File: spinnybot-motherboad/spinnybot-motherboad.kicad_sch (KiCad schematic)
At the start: 6 parts

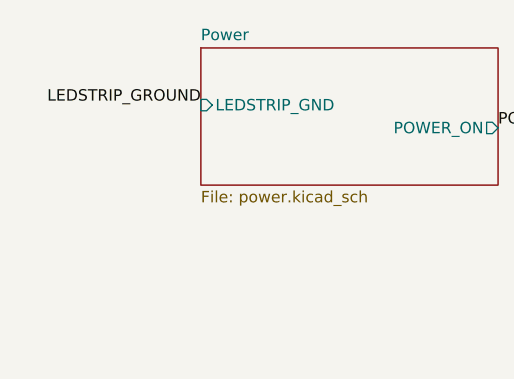
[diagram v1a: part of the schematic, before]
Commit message: fix LEDSTRIP_GND on the FET not being connected
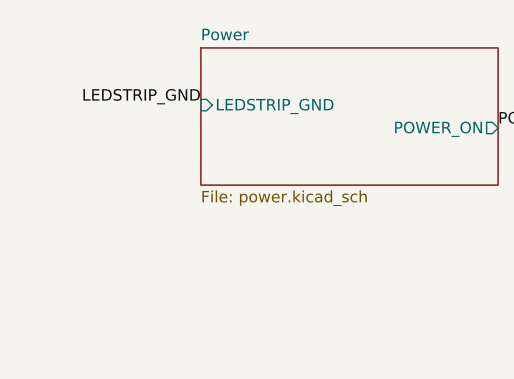
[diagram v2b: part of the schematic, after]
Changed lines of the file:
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@@
     (effects (font (size 1.27 1.27)) (justify left bottom))
   )
-  (label "LEDSTRIP_GROUND" (at 34.29 30.48 180)
+  (label "LEDSTRIP_GND" (at 34.29 30.48 180)
     (effects (font (size 1.27 1.27)) (justify right bottom))
   )

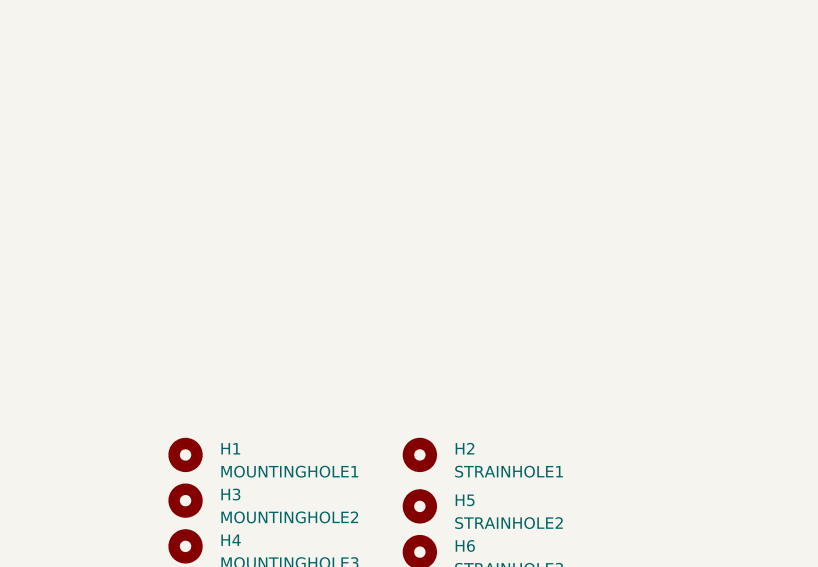
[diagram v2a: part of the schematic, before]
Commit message: tweaks to routing to make the ground plane more connected, add a top copper ground pour. move ESC FET.
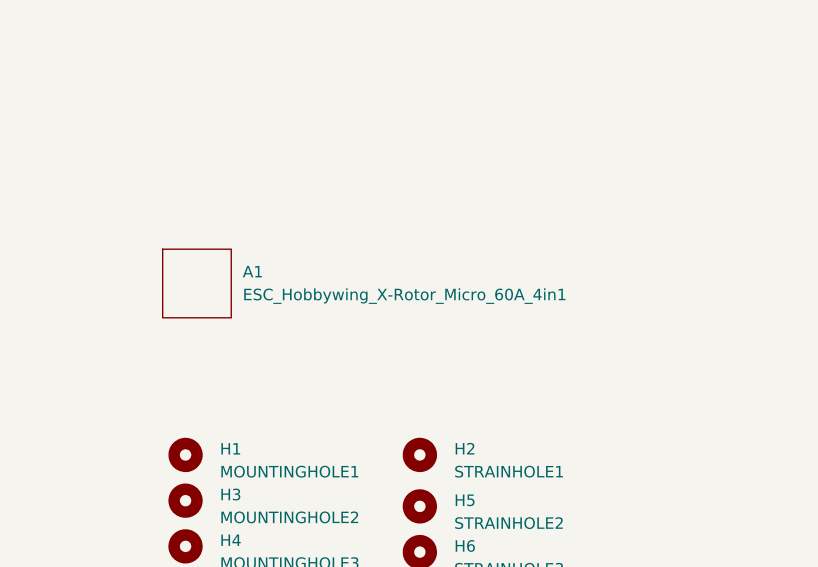
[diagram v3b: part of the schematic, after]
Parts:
- added A1: ESC_Hobbywing_X-Rotor_Micro_60A_4in1, esc_4in1:ESC_Hobbywing_X-Rotor_Micro_60A_4in1, symbol esc_4in1:ESC_Hobbywing_X-Rotor_Micro_60A_4in1
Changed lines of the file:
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@@
+    )
+  )
+  (symbol (lib_id "esc_4in1:ESC_Hobbywing_X-Rotor_Micro_60A_4in1") (at 50.8 134.62 0) (unit 1)
+    (in_bom yes) (on_board yes) (fields_autoplaced)
+    (property "Reference" "A1" (id 0) (at 55.88 133.3499 0)
+      (effects (font (size 1.27 1.27)) (justify left))
+    )
+    (property "Value" "ESC_Hobbywing_X-Rotor_Micro_60A_4in1" (id 1) (at 55.88 135.8899 0)
+      (effects (font (size 1.27 1.27)) (justify left))
+    )
+    (property "Footprint" "esc_4in1:ESC_Hobbywing_X-Rotor_Micro_60A_4in1" (id 2) (at 50.8 134.62 0)
+      (effects (font (size 1.27 1.27)) hide)
+    )
+    (property "Datasheet" "" (id 3) (at 50.8 134.62 0)
+      (effects (font (size 1.27 1.27)) hide)
     )
   )
@@
       (reference "#PWR0165") (unit 1) (value "GND") (footprint "")
     )
+    (path "/dd1316dc-7e5b-4c97-959e-6f6a1eeeb379/63151d2c-c4e6-4f75-94c3-ad61a0505834"
+      (reference "#PWR0166") (unit 1) (value "GND") (footprint "")
+    )
+    (path "/dd1316dc-7e5b-4c97-959e-6f6a1eeeb379/b6338eda-846c-4d61-9775-8bb6d52342a5"
+      (reference "#PWR0167") (unit 1) (value "GND") (footprint "")
+    )
+    (path "/4b51d6df-63b9-43fa-a920-8afa01c20793"
+      (reference "A1") (unit 1) (value "ESC_Hobbywing_X-Rotor_Micro_60A_4in1") (footprint "esc_4in1:ESC_Hobbywing_X-Rotor_Micro_60A_4in1")
+    )
     (path "/dd1316dc-7e5b-4c97-959e-6f6a1eeeb379/b5ccd461-2bb6-4e55-889d-c413ead53e97"

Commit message: adjust mounting holes to have pads and change locations
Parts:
- H2, H5, H6: footprint custom:MountingHole_3.3mm -> custom:StrainHole_3.3mm
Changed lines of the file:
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@@
       (effects (font (size 1.27 1.27)) (justify right))
     )
-    (property "Footprint" "custom:MountingHole_3.3mm" (id 2) (at 75.565 159.385 0)
+    (property "Footprint" "custom:StrainHole_3.3mm" (id 2) (at 75.565 159.385 0)
       (effects (font (size 1.27 1.27)) hide)
     )
@@
       (effects (font (size 1.27 1.27)) (justify right))
     )
-    (property "Footprint" "custom:MountingHole_3.3mm" (id 2) (at 75.565 153.67 0)
+    (property "Footprint" "custom:StrainHole_3.3mm" (id 2) (at 75.565 153.67 0)
       (effects (font (size 1.27 1.27)) hide)
     )
@@
       (effects (font (size 1.27 1.27)) (justify right))
     )
-    (property "Footprint" "custom:MountingHole_3.3mm" (id 2) (at 75.565 164.465 0)
+    (property "Footprint" "custom:StrainHole_3.3mm" (id 2) (at 75.565 164.465 0)
       (effects (font (size 1.27 1.27)) hide)
     )
@@
     )
     (path "/90a0860f-dc0f-486d-8126-ac86f257452e"
-      (reference "H2") (unit 1) (value "STRAINHOLE1") (footprint "custom:MountingHole_3.3mm")
+      (reference "H2") (unit 1) (value "STRAINHOLE1") (footprint "custom:StrainHole_3.3mm")
     )
     (path "/4daec26f-7303-4f29-a6dc-74eca012aa20"
@@
     )
     (path "/44671e4b-c3f2-40ce-9f5f-ae56c7ceee2e"
-      (reference "H5") (unit 1) (value "STRAINHOLE2") (footprint "custom:MountingHole_3.3mm")
+      (reference "H5") (unit 1) (value "STRAINHOLE2") (footprint "custom:StrainHole_3.3mm")
     )
     (path "/b2df31ea-f8d8-459e-bfc0-eb9493f3925c"
-      (reference "H6") (unit 1) (value "STRAINHOLE3") (footprint "custom:MountingHole_3.3mm")
+      (reference "H6") (unit 1) (value "STRAINHOLE3") (footprint "custom:StrainHole_3.3mm")
     )
     (path "/ce9f0f17-1862-4671-a57d-feb3cf47b091/205531ef-2109-472f-bb9a-44bf26b6d265"

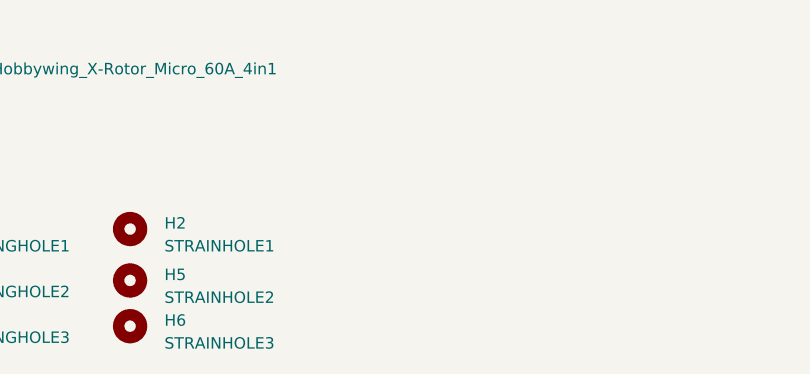
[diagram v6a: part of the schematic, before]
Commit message: add extra strain relief holes back in the original locations
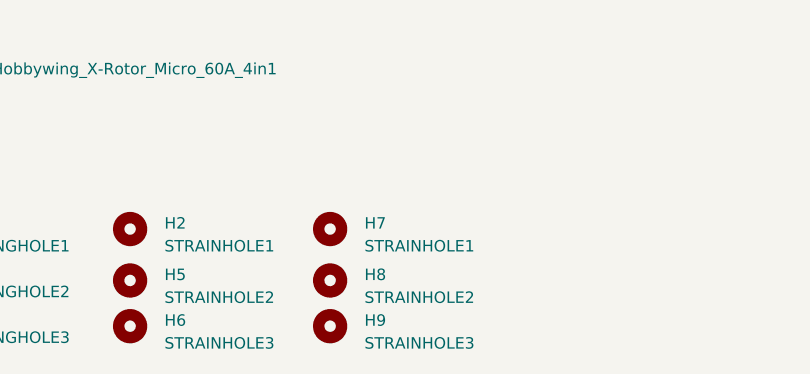
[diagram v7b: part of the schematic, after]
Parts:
- added H7: STRAINHOLE1, custom:StrainHole_3.3mm, symbol Mechanical:MountingHole
- added H8: STRAINHOLE2, custom:StrainHole_3.3mm, symbol Mechanical:MountingHole
- added H9: STRAINHOLE3, custom:StrainHole_3.3mm, symbol Mechanical:MountingHole
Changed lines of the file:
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@@
     (effects (font (size 1.27 1.27)) (justify right bottom))
+  )
+  (symbol (lib_id "Mechanical:MountingHole") (at 97.79 153.67 90) (unit 1)
+    (in_bom yes) (on_board yes)
+    (property "Reference" "H7" (id 0) (at 101.6 153.0349 90)
+      (effects (font (size 1.27 1.27)) (justify right))
+    )
+    (property "Value" "STRAINHOLE1" (id 1) (at 101.6 155.5749 90)
+      (effects (font (size 1.27 1.27)) (justify right))
+    )
+    (property "Footprint" "custom:StrainHole_3.3mm" (id 2) (at 97.79 153.67 0)
+      (effects (font (size 1.27 1.27)) hide)
+    )
+    (property "Datasheet" "~" (id 3) (at 97.79 153.67 0)
+      (effects (font (size 1.27 1.27)) hide)
+    )
+  )
+  (symbol (lib_id "Mechanical:MountingHole") (at 97.79 159.385 90) (unit 1)
+    (in_bom yes) (on_board yes)
+    (property "Reference" "H8" (id 0) (at 101.6 158.7499 90)
+      (effects (font (size 1.27 1.27)) (justify right))
+    )
+    (property "Value" "STRAINHOLE2" (id 1) (at 101.6 161.2899 90)
+      (effects (font (size 1.27 1.27)) (justify right))
+    )
+    (property "Footprint" "custom:StrainHole_3.3mm" (id 2) (at 97.79 159.385 0)
+      (effects (font (size 1.27 1.27)) hide)
+    )
+    (property "Datasheet" "~" (id 3) (at 97.79 159.385 0)
+      (effects (font (size 1.27 1.27)) hide)
+    )
   )
   (symbol (lib_id "Mechanical:MountingHole") (at 49.53 153.67 90) (unit 1)
@@
     )
     (property "Datasheet" "~" (id 3) (at 49.53 158.75 0)
+      (effects (font (size 1.27 1.27)) hide)
+    )
+  )
+  (symbol (lib_id "Mechanical:MountingHole") (at 97.79 164.465 90) (unit 1)
+    (in_bom yes) (on_board yes)
+    (property "Reference" "H9" (id 0) (at 101.6 163.8299 90)
+      (effects (font (size 1.27 1.27)) (justify right))
+    )
+    (property "Value" "STRAINHOLE3" (id 1) (at 101.6 166.3699 90)
+      (effects (font (size 1.27 1.27)) (justify right))
+    )
+    (property "Footprint" "custom:StrainHole_3.3mm" (id 2) (at 97.79 164.465 0)
+      (effects (font (size 1.27 1.27)) hide)
+    )
+    (property "Datasheet" "~" (id 3) (at 97.79 164.465 0)
       (effects (font (size 1.27 1.27)) hide)
     )
@@
       (reference "H6") (unit 1) (value "STRAINHOLE3") (footprint "custom:StrainHole_3.3mm")
     )
+    (path "/12290910-e1c4-4f12-a089-9b99be24c1fc"
+      (reference "H7") (unit 1) (value "STRAINHOLE1") (footprint "custom:StrainHole_3.3mm")
+    )
+    (path "/149f0dc4-9b74-4a1a-a37b-7eb355956a7a"
+      (reference "H8") (unit 1) (value "STRAINHOLE2") (footprint "custom:StrainHole_3.3mm")
+    )
+    (path "/59005896-4816-4eaa-bcde-06df3c15d37e"
+      (reference "H9") (unit 1) (value "STRAINHOLE3") (footprint "custom:StrainHole_3.3mm")
+    )
     (path "/ce9f0f17-1862-4671-a57d-feb3cf47b091/205531ef-2109-472f-bb9a-44bf26b6d265"

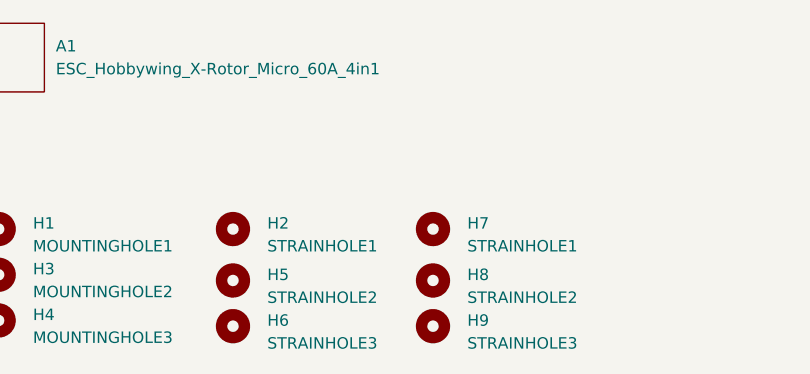
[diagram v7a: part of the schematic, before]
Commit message: adjust board to use new outline with bottom edge closer to center
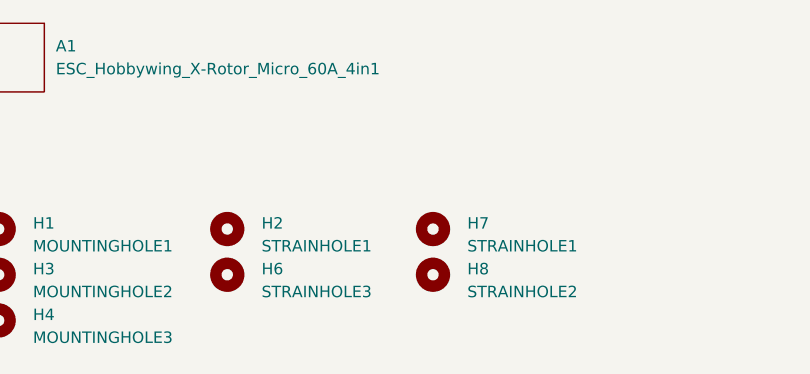
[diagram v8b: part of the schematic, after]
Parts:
- removed H5: STRAINHOLE2, custom:StrainHole_3.3mm, symbol Mechanical:MountingHole
- removed H9: STRAINHOLE3, custom:StrainHole_3.3mm, symbol Mechanical:MountingHole
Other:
- moved on the sheet: H2, H6, H8
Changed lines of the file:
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@@
     )
   )
-  (symbol (lib_id "Mechanical:MountingHole") (at 97.79 159.385 90) (unit 1)
+  (symbol (lib_id "Mechanical:MountingHole") (at 97.79 158.75 90) (unit 1)
     (in_bom yes) (on_board yes)
-    (property "Reference" "H8" (id 0) (at 101.6 158.7499 90)
-      (effects (font (size 1.27 1.27)) (justify right))
-    )
-    (property "Value" "STRAINHOLE2" (id 1) (at 101.6 161.2899 90)
-      (effects (font (size 1.27 1.27)) (justify right))
-    )
-    (property "Footprint" "custom:StrainHole_3.3mm" (id 2) (at 97.79 159.385 0)
-      (effects (font (size 1.27 1.27)) hide)
-    )
-    (property "Datasheet" "~" (id 3) (at 97.79 159.385 0)
+    (property "Reference" "H8" (id 0) (at 101.6 158.1149 90)
+      (effects (font (size 1.27 1.27)) (justify right))
+    )
+    (property "Value" "STRAINHOLE2" (id 1) (at 101.6 160.6549 90)
+      (effects (font (size 1.27 1.27)) (justify right))
+    )
+    (property "Footprint" "custom:StrainHole_3.3mm" (id 2) (at 97.79 158.75 0)
+      (effects (font (size 1.27 1.27)) hide)
+    )
+    (property "Datasheet" "~" (id 3) (at 97.79 158.75 0)
       (effects (font (size 1.27 1.27)) hide)
     )
@@
     )
   )
-  (symbol (lib_id "Mechanical:MountingHole") (at 75.565 159.385 90) (unit 1)
-    (in_bom yes) (on_board yes)
-    (property "Reference" "H5" (id 0) (at 79.375 158.7499 90)
-      (effects (font (size 1.27 1.27)) (justify right))
-    )
-    (property "Value" "STRAINHOLE2" (id 1) (at 79.375 161.2899 90)
-      (effects (font (size 1.27 1.27)) (justify right))
-    )
-    (property "Footprint" "custom:StrainHole_3.3mm" (id 2) (at 75.565 159.385 0)
-      (effects (font (size 1.27 1.27)) hide)
-    )
-    (property "Datasheet" "~" (id 3) (at 75.565 159.385 0)
-      (effects (font (size 1.27 1.27)) hide)
-    )
-  )
   (symbol (lib_id "Mechanical:MountingHole") (at 49.53 163.83 90) (unit 1)
     (in_bom yes) (on_board yes)
@@
     )
   )
-  (symbol (lib_id "Mechanical:MountingHole") (at 97.79 164.465 90) (unit 1)
+  (symbol (lib_id "Mechanical:MountingHole") (at 74.93 153.67 90) (unit 1)
     (in_bom yes) (on_board yes)
-    (property "Reference" "H9" (id 0) (at 101.6 163.8299 90)
-      (effects (font (size 1.27 1.27)) (justify right))
-    )
-    (property "Value" "STRAINHOLE3" (id 1) (at 101.6 166.3699 90)
-      (effects (font (size 1.27 1.27)) (justify right))
-    )
-    (property "Footprint" "custom:StrainHole_3.3mm" (id 2) (at 97.79 164.465 0)
-      (effects (font (size 1.27 1.27)) hide)
-    )
-    (property "Datasheet" "~" (id 3) (at 97.79 164.465 0)
-      (effects (font (size 1.27 1.27)) hide)
-    )
-  )
-  (symbol (lib_id "Mechanical:MountingHole") (at 75.565 153.67 90) (unit 1)
+    (property "Reference" "H2" (id 0) (at 78.74 153.0349 90)
+      (effects (font (size 1.27 1.27)) (justify right))
+    )
+    (property "Value" "STRAINHOLE1" (id 1) (at 78.74 155.5749 90)
+      (effects (font (size 1.27 1.27)) (justify right))
+    )
+    (property "Footprint" "custom:StrainHole_3.3mm" (id 2) (at 74.93 153.67 0)
+      (effects (font (size 1.27 1.27)) hide)
+    )
+    (property "Datasheet" "~" (id 3) (at 74.93 153.67 0)
+      (effects (font (size 1.27 1.27)) hide)
+    )
+  )
+  (symbol (lib_id "Mechanical:MountingHole") (at 74.93 158.75 90) (unit 1)
     (in_bom yes) (on_board yes)
-    (property "Reference" "H2" (id 0) (at 79.375 153.0349 90)
-      (effects (font (size 1.27 1.27)) (justify right))
-    )
-    (property "Value" "STRAINHOLE1" (id 1) (at 79.375 155.5749 90)
-      (effects (font (size 1.27 1.27)) (justify right))
-    )
-    (property "Footprint" "custom:StrainHole_3.3mm" (id 2) (at 75.565 153.67 0)
-      (effects (font (size 1.27 1.27)) hide)
-    )
-    (property "Datasheet" "~" (id 3) (at 75.565 153.67 0)
-      (effects (font (size 1.27 1.27)) hide)
-    )
-  )
-  (symbol (lib_id "Mechanical:MountingHole") (at 75.565 164.465 90) (unit 1)
-    (in_bom yes) (on_board yes)
-    (property "Reference" "H6" (id 0) (at 79.375 163.8299 90)
-      (effects (font (size 1.27 1.27)) (justify right))
-    )
-    (property "Value" "STRAINHOLE3" (id 1) (at 79.375 166.3699 90)
-      (effects (font (size 1.27 1.27)) (justify right))
-    )
-    (property "Footprint" "custom:StrainHole_3.3mm" (id 2) (at 75.565 164.465 0)
-      (effects (font (size 1.27 1.27)) hide)
-    )
-    (property "Datasheet" "~" (id 3) (at 75.565 164.465 0)
+    (property "Reference" "H6" (id 0) (at 78.74 158.1149 90)
+      (effects (font (size 1.27 1.27)) (justify right))
+    )
+    (property "Value" "STRAINHOLE3" (id 1) (at 78.74 160.6549 90)
+      (effects (font (size 1.27 1.27)) (justify right))
+    )
+    (property "Footprint" "custom:StrainHole_3.3mm" (id 2) (at 74.93 158.75 0)
+      (effects (font (size 1.27 1.27)) hide)
+    )
+    (property "Datasheet" "~" (id 3) (at 74.93 158.75 0)
       (effects (font (size 1.27 1.27)) hide)
     )
@@
       (reference "H4") (unit 1) (value "MOUNTINGHOLE3") (footprint "custom:MountingHole_3.3mm")
     )
-    (path "/44671e4b-c3f2-40ce-9f5f-ae56c7ceee2e"
-      (reference "H5") (unit 1) (value "STRAINHOLE2") (footprint "custom:StrainHole_3.3mm")
-    )
     (path "/b2df31ea-f8d8-459e-bfc0-eb9493f3925c"
       (reference "H6") (unit 1) (value "STRAINHOLE3") (footprint "custom:StrainHole_3.3mm")
@@
       (reference "H8") (unit 1) (value "STRAINHOLE2") (footprint "custom:StrainHole_3.3mm")
     )
-    (path "/59005896-4816-4eaa-bcde-06df3c15d37e"
-      (reference "H9") (unit 1) (value "STRAINHOLE3") (footprint "custom:StrainHole_3.3mm")
-    )
     (path "/ce9f0f17-1862-4671-a57d-feb3cf47b091/205531ef-2109-472f-bb9a-44bf26b6d265"
